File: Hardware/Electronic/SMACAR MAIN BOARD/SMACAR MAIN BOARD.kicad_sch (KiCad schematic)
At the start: 10 parts, among them J2 USB_C_Receptacle_USB2.0_14P, U2 ESP32-S3-DevKitC

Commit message: upgrade
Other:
- company: (none) -> Instituto Tecnologico de las Americas
- title: (none) -> Placa de control transmisora
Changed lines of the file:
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@@
 	(generator_version "9.0")
 	(paper "A4")
+	(title_block
+		(title "Placa de control transmisora")
+		(rev "Camila F. Vargas")
+		(company "Instituto Tecnologico de las Americas")
+	)
 	(rectangle
 		(start 220.98 82.55)

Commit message: Placa Terminada y Revisada por Camila Fernandez
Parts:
- removed R1, R2: 5.6k, Resistor_THT:R_Axial_DIN0207_L6.3mm_D2.5mm_P10.16mm_Horizontal, symbol PCM_SL_Resistors:5.6k
- removed Z1: DIODE_ZENER, symbol freetronics_schematic:DIODE_ZENER
- added R1_5.6k1, R2_5.6k1, R3_10k1, R4_10k1: 470R_0805_350mW, PCM_4ms_Resistor:R_0805_2012Metric, symbol PCM_4ms_Resistor:470R_0805_350mW
- MOLEX1: value M03PTH -> ELECTRICAL CONDUCTIVITY SENSOR
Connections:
- net 5V: now also J2.A4 (VBUS), J2.A9 (VBUS), J2.B4 (VBUS), J2.B9 (VBUS)
- net GND: now also R1_5.6k1.2, R2_5.6k1.2
- net SCL: now also R3_10k1.1
- net SDA: now also R4_10k1.1
- net at J2.A5 (CC1): now also R1_5.6k1.1
- net at J2.B5 (CC2): now also R2_5.6k1.1
- net at U2.1 (3V3), U2.2 (3V3): now also R3_10k1.2, R4_10k1.2
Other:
- note added: "MICROCONTROLADOR"

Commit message: TVS
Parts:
- added U1, U3: TVS0500DRV, Package_SON:WSON-6-1EP_2x2mm_P0.65mm_EP1x1.6mm, symbol Power_Protection:TVS0500DRV
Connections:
- net 5V: now also U1.4 (IN), U1.5 (IN), U1.6 (IN)
- net GND: now also U1.1 (GND), U1.2 (GND), U1.3 (GND), U1.7 (GND), U3.1 (GND), U3.2 (GND), U3.3 (GND), U3.7 (GND)
- net at R3_10k1.2, R4_10k1.2, U2.1 (3V3)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: now also U3.4 (IN), U3.5 (IN), U3.6 (IN)

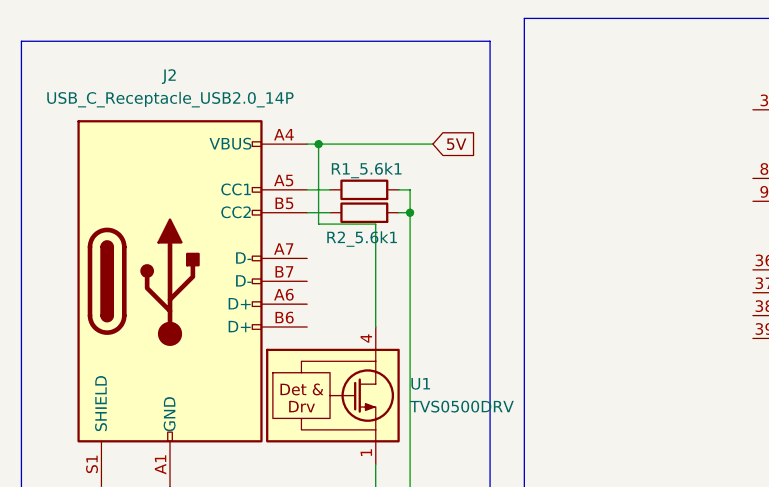
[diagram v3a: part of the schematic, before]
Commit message: RESISTENCIA PULL DOWN 5.1K
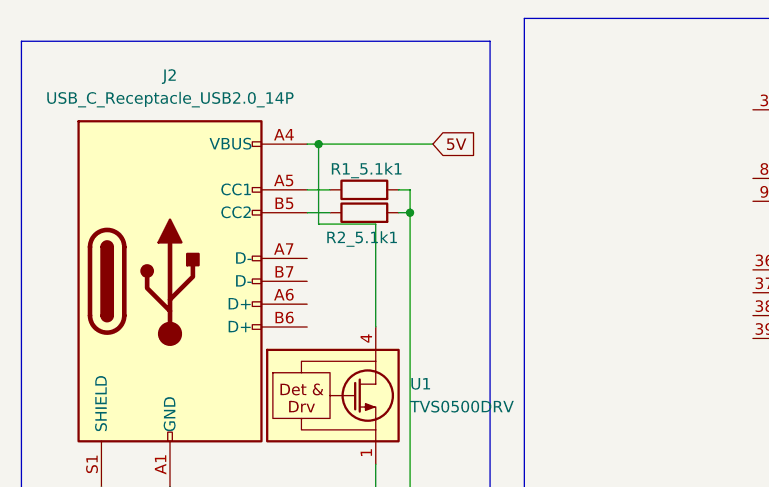
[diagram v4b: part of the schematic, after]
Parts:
- renumbered R1_5.6k1 to R1_5.1k1, R2_5.6k1 to R2_5.1k1
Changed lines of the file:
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@@
 		(on_board yes)
 		(dnp no)
-		(property "Reference" "R2_5.6k1"
+		(property "Reference" "R2_5.1k1"
 			(at 78.486 38.354 90)
 			(effects
@@
 			(project "SMACAR MAIN BOARD"
 				(path "/4878f518-0ef3-4f65-a6b2-5ae917900823"
-					(reference "R2_5.6k1")
+					(reference "R2_5.1k1")
 					(unit 1)
 				)
@@
 		(on_board yes)
 		(dnp no)
-		(property "Reference" "R1_5.6k1"
+		(property "Reference" "R1_5.1k1"
 			(at 78.994 30.734 90)
 			(effects
@@
 			(project ""
 				(path "/4878f518-0ef3-4f65-a6b2-5ae917900823"
-					(reference "R1_5.6k1")
+					(reference "R1_5.1k1")
 					(unit 1)
 				)

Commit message: V1.0 Revision
Revision for V1.0 of the project. Includes production files for JLCPCB. Some footprints and schematic symbols were changed.
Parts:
- removed J2: USB_C_Receptacle_USB2.0_14P, Connector_USB:USB_C_Receptacle_GCT_USB4105-xx-A_16P_TopMnt_Horizontal, symbol Connector:USB_C_Receptacle_USB2.0_14P
- removed U1, U3: TVS0500DRV, Package_SON:WSON-6-1EP_2x2mm_P0.65mm_EP1x1.6mm, symbol Power_Protection:TVS0500DRV
- added D1, D2: SMF33A, Diode_SMD:D_SMF, symbol Diode:SMF33A
- added J2: 2137160001, XUNPU TYPEC-306DDW-ARP16:MOLEX_2137160001, symbol XUNPU TYPEC-306DDW-ARP16:2137160001
- R1_5.1k1, R2_5.1k1, R3_10k1, R4_10k1: footprint PCM_4ms_Resistor:R_0805_2012Metric -> Resistor_SMD:R_0805_2012Metric_Pad1.20x1.40mm_HandSolder
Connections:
- net 5V is gone; now on net +5V: MOLEX1.2, MOLEX2.2, MOLEX3.2, MOLEX4.2, MOLEX5.1, U2.21 (5V)
- net GND: now also D1.2 (A2), D2.2 (A2), J2.A1 (GND1), J2.A12 (GND2), J2.B1 (GND3), J2.B12 (GND4), J2.SH1 (SHIELD1), J2.SH2 (SHIELD2), J2.SH3 (SHIELD3), J2.SH4 (SHIELD4); no longer R1_5.1k1.2, R2_5.1k1.2
- net +5V: now reaches R2_5.1k1.1
- net +5V: now also R1_5.1k1.2, D1.1 (A1), J2.A4 (VBUS1), J2.A9 (VBUS2), J2.B4 (VBUS3), J2.B9 (VBUS4)
- net at R3_10k1.2, R4_10k1.2, U2.1 (3V3)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: now also D2.1 (A1)
- net at R1_5.1k1.1: now also J2.B5 (CC2)
- new net: J2.A5 (CC1), R2_5.1k1.2
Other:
- moved on the sheet: R1_5.1k1, R2_5.1k1

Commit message: update
PCB Y CODIGO PROTOTIPO
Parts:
- removed D1, D2: SMF33A, Diode_SMD:D_SMF, symbol Diode:SMF33A
- removed J2: 2137160001, XUNPU TYPEC-306DDW-ARP16:MOLEX_2137160001, symbol XUNPU TYPEC-306DDW-ARP16:2137160001
- removed R1_5.1k1, R2_5.1k1: 470R_0805_350mW, Resistor_SMD:R_0805_2012Metric_Pad1.20x1.40mm_HandSolder, symbol PCM_4ms_Resistor:470R_0805_350mW
- added J2: Conn_01x02, Connector_Molex:Molex_KK-254_AE-6410-02A_1x02_P2.54mm_Vertical, symbol SparkFun-Connector:Conn_01x02
- added R1: 4.7k, SparkFun-Resistor:R_0603_1608Metric, symbol SparkFun-Resistor:4.7k_0603
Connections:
- net +5V: now also J2.2 (Pin_2)
- net GND: now also J2.1 (Pin_1)
- net TEMP SENSOR: now also U2.31 (GPIO0), R1.1; no longer U2.27 (GPIO21)
- net at R3_10k1.2, R4_10k1.2, U2.1 (3V3)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: now also R1.2

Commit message: cosillas
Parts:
- removed R3_10k1, R4_10k1: 470R_0805_350mW, Resistor_SMD:R_0805_2012Metric_Pad1.20x1.40mm_HandSolder, symbol PCM_4ms_Resistor:470R_0805_350mW
- R1: footprint SparkFun-Resistor:R_0603_1608Metric -> Resistor_THT:R_Axial_DIN0204_L3.6mm_D1.6mm_P7.62mm_Horizontal
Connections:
- net Tx: now reaches U2.10 (GPIO17/ADC2_CH6)
- net Tx: now also MOLEX5.4
- net RX: now reaches U2.9 (GPIO16/ADC2_CH5/32K_N)
- net RX: now also MOLEX5.3
- net SCL: no longer names the net of U2.15 (GPIO9/ADC1_CH8)
- net SCL: no longer MOLEX5.3
- net SDA: no longer names the net of U2.12 (GPIO8/ADC1_CH7)
- net SDA: no longer MOLEX5.4

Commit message: PCBS
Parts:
- added C1, C2, C3: 100nF_Ceramic, Capacitor_THT:C_Disc_D5.0mm_W2.5mm_P2.50mm, symbol PCM_SL_Capacitors:100nF_Ceramic
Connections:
- net +5V: no longer MOLEX4.2
- net ELECTRICAL CONDUCTIVITY: now also C1.1
- net GND: now also C1.2, C2.2, C3.2
- net PH SENSOR: now also C2.1
- net TDS SENSOR: now also C3.1
- net 3.3V: now reaches R1.2, U2.1 (3V3), U2.2 (3V3)
- net 3.3V: now also MOLEX4.2
